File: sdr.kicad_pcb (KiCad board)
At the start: 4 copper layers, 65 x 30 mm, 136 parts, among them U1 FT601, U10 MIC94310, U11 PAM2305, U2 ESD7016, U3 LMS6002DR2, U4 ECP5, U5 Si5351, U6 PAM2305, U7 NCP186, U8 MIC94310, U9 MIC94310, X1 GSB443133HR, X2 CONN_01X08, X3 RaspberryPiConnector, Y1 FL3000027, Y2 ABM11-141-26.000MHZ

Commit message: All traced except Rpi and LMS
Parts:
- moved R6 6.61 mm to (124.7, 123.5)
- moved C77 2.49 mm to (153.6, 111.7)
- moved R7 1.64 mm to (125.1, 126.0)
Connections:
- net Net-(X3-Pad25) renamed /RPi/~RPI_WE
- net Net-(X3-Pad32) renamed /RPi/~RPI_OE
- U4 pad T17: /FT601/I2C_SCL -> Net-(U4-PadT17)
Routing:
- net ~CFG_HOLD: track 0.00 -> 74.0 mm, vias 0 -> 1
- net FT_GPIO1: track 19.5 -> 75.5 mm, vias 2 -> 3
- net LMS_D3V3: track 88.5 -> 125.4 mm, vias 17 -> 22
- net RPI_D13: track 0.00 -> 26.0 mm
- net CFG_MCLK: track 0.00 -> 25.1 mm, vias 0 -> 1
- net CFG_MISO: track 0.00 -> 23.5 mm, vias 0 -> 1
- net CFG_MOSI: track 0.00 -> 22.4 mm, vias 0 -> 1
- net RPI_D8: track 0.00 -> 21.8 mm
- net RPI_D12: track 0.00 -> 21.5 mm
- net RPI_D4: track 0.00 -> 19.2 mm
- net RPI_D11: track 0.00 -> 19.1 mm
- net RPI_D5: track 0.00 -> 18.6 mm
- net GNDD: track 235.4 -> 252.1 mm, vias 102 -> 104
- net /RPi/~RPI_OE: track 0.00 -> 15.6 mm
- net RPI_A4: track 0.00 -> 13.8 mm
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- added copper zone on F.Cu, net GNDD

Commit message: RPI is almost finished
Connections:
- U4 pad A10: Net-(U4-PadA10) -> RPI_D14
- U4 pad A11: Net-(U4-PadA11) -> RPI_D17
- U4 pad A12: Net-(U4-PadA12) -> RPI_A0
- U4 pad A13: Net-(U4-PadA13) -> /RPi/~RPI_OE
- U4 pad A14: Net-(U4-PadA14) -> RPI_D8
- U4 pad A16: Net-(U4-PadA16) -> RPI_D12
- U4 pad A7: Net-(U4-PadA7) -> RPI_A1
- U4 pad A8: Net-(U4-PadA8) -> RPI_D7
- U4 pad A9: Net-(U4-PadA9) -> RPI_D10
- U4 pad B11: Net-(U4-PadB11) -> RPI_D15
- U4 pad B12: Net-(U4-PadB12) -> RPI_A4
- U4 pad B13: Net-(U4-PadB13) -> RPI_D5
- U4 pad B16: Net-(U4-PadB16) -> RPI_D11
- U4 pad B8: Net-(U4-PadB8) -> RPI_D6
- U4 pad B9: Net-(U4-PadB9) -> RPI_D9
- U4 pad C10: Net-(U4-PadC10) -> RPI_GPIO1
- U4 pad C13: Net-(U4-PadC13) -> RPI_D4
- U4 pad E17: Net-(U4-PadE17) -> RPI_D13
- U4 pad F18: Net-(U4-PadF18) -> RPI_A5
- U4 pad G16: Net-(U4-PadG16) -> ~RPI_WE
- X3 pad 25: /RPi/~RPI_WE -> ~RPI_WE
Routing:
- net RPI_D6: track 0.00 -> 21.0 mm
- net RPI_D7: track 0.00 -> 18.0 mm
- net RPI_A1: track 0.00 -> 17.3 mm
- net RPI_D10: track 0.00 -> 16.5 mm
- net RPI_D9: track 0.00 -> 15.4 mm
- net RPI_A5: track 0.00 -> 14.5 mm, vias 0 -> 1
- net RPI_GPIO1: track 0.00 -> 14.2 mm
- net RPI_D15: track 0.00 -> 13.7 mm
- net ~RPI_WE: track 0.00 -> 13.4 mm, vias 0 -> 1
- net Net-(U4-PadF17): track 11.2 -> 0.02 mm, vias 1 -> 0
- net RPI_D14: track 0.00 -> 10.4 mm
- net Net-(U4-PadG18): track 9.79 -> 0.02 mm, vias 1 -> 0
- net RPI_D17: track 0.00 -> 8.65 mm
- net FT_GPIO1: track 75.5 -> 79.2 mm
- net RPI_CNTD: track 64.4 -> 66.5 mm
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
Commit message: Everything is done except LMS and RF
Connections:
- U4 pad A10: RPI_D14 -> RPI_GPIO1
- U4 pad A11: RPI_D17 -> RPI_D15
- U4 pad A12: RPI_A0 -> RPI_D17
- U4 pad A13: /RPi/~RPI_OE -> RPI_D4
- U4 pad A2: Net-(U4-PadA2) -> (no net)
- U4 pad A3: Net-(U4-PadA3) -> (no net)
- U4 pad A4: Net-(U4-PadA4) -> (no net)
- U4 pad A5: Net-(U4-PadA5) -> (no net)
- U4 pad A7: RPI_A1 -> RPI_A2
- U4 pad A8: RPI_D7 -> RPI_D6
- U4 pad A9: RPI_D10 -> RPI_D9
- U4 pad B1: Net-(U4-PadB1) -> (no net)
- U4 pad B10: Net-(U4-PadB10) -> RPI_D10
- U4 pad B11: RPI_D15 -> RPI_D14
- U4 pad B12: RPI_A4 -> RPI_D16
- U4 pad B15: Net-(U4-PadB15) -> RPI_A4
- U4 pad B2: Net-(U4-PadB2) -> (no net)
- U4 pad B3: Net-(U4-PadB3) -> (no net)
- U4 pad B4: Net-(U4-PadB4) -> (no net)
- U4 pad B5: Net-(U4-PadB5) -> (no net)
- U4 pad B8: RPI_D6 -> RPI_A1
- U4 pad B9: RPI_D9 -> RPI_D7
- U4 pad C1: Net-(U4-PadC1) -> (no net)
- U4 pad C10: RPI_GPIO1 -> Net-(U4-PadC10)
- U4 pad C13: RPI_D4 -> RPI_A0
- U4 pad C2: Net-(U4-PadC2) -> (no net)
- U4 pad C3: Net-(U4-PadC3) -> (no net)
- U4 pad C4: Net-(U4-PadC4) -> (no net)
- U4 pad C5: Net-(U4-PadC5) -> (no net)
- U4 pad C6: Net-(U4-PadC6) -> RPI_A3
- U4 pad D1: Net-(U4-PadD1) -> (no net)
- U4 pad D11: Net-(U4-PadD11) -> /RPi/~RPI_WE
- U4 pad D2: Net-(U4-PadD2) -> (no net)
- U4 pad D3: Net-(U4-PadD3) -> (no net)
- U4 pad D5: Net-(U4-PadD5) -> (no net)
- U4 pad E1: Net-(U4-PadE1) -> (no net)
- U4 pad E2: Net-(U4-PadE2) -> (no net)
- U4 pad E3: Net-(U4-PadE3) -> (no net)
- U4 pad E4: Net-(U4-PadE4) -> (no net)
- U4 pad E5: Net-(U4-PadE5) -> (no net)
- U4 pad F1: Net-(U4-PadF1) -> (no net)
- U4 pad F18: RPI_A5 -> ~RPI_OE
- U4 pad F2: Net-(U4-PadF2) -> (no net)
- U4 pad F3: Net-(U4-PadF3) -> (no net)
- U4 pad F4: Net-(U4-PadF4) -> (no net)
- U4 pad F5: Net-(U4-PadF5) -> (no net)
- U4 pad G1: Net-(U4-PadG1) -> (no net)
- U4 pad G16: ~RPI_WE -> RPI_A5
- U4 pad G2: Net-(U4-PadG2) -> (no net)
- U4 pad G3: Net-(U4-PadG3) -> (no net)
- U4 pad G5: Net-(U4-PadG5) -> (no net)
- U4 pad H1: Net-(U4-PadH1) -> (no net)
- U4 pad H2: Net-(U4-PadH2) -> (no net)
- U4 pad H3: Net-(U4-PadH3) -> (no net)
- U4 pad H4: Net-(U4-PadH4) -> (no net)
- U4 pad H5: Net-(U4-PadH5) -> (no net)
- U4 pad J1: Net-(U4-PadJ1) -> (no net)
- U4 pad J3: Net-(U4-PadJ3) -> (no net)
- U4 pad J4: Net-(U4-PadJ4) -> (no net)
- U4 pad J5: Net-(U4-PadJ5) -> (no net)
- U4 pad K1: Net-(U4-PadK1) -> (no net)
- U4 pad K2: Net-(U4-PadK2) -> (no net)
- U4 pad K3: Net-(U4-PadK3) -> (no net)
- U4 pad K4: Net-(U4-PadK4) -> (no net)
- U4 pad K5: Net-(U4-PadK5) -> (no net)
- U4 pad L1: Net-(U4-PadL1) -> (no net)
- U4 pad L2: Net-(U4-PadL2) -> (no net)
- U4 pad L3: Net-(U4-PadL3) -> (no net)
- U4 pad L4: Net-(U4-PadL4) -> (no net)
- U4 pad L5: Net-(U4-PadL5) -> (no net)
- U4 pad M1: Net-(U4-PadM1) -> (no net)
- U4 pad M3: Net-(U4-PadM3) -> (no net)
- U4 pad M4: Net-(U4-PadM4) -> (no net)
- U4 pad N1: Net-(U4-PadN1) -> (no net)
- U4 pad N2: Net-(U4-PadN2) -> (no net)
- U4 pad N3: Net-(U4-PadN3) -> (no net)
- U4 pad N4: Net-(U4-PadN4) -> (no net)
- U4 pad N5: Net-(U4-PadN5) -> (no net)
- U4 pad P1: Net-(U4-PadP1) -> (no net)
- U4 pad P2: Net-(U4-PadP2) -> (no net)
- U4 pad P3: Net-(U4-PadP3) -> (no net)
- U4 pad P4: Net-(U4-PadP4) -> (no net)
- U4 pad P5: Net-(U4-PadP5) -> (no net)
- U4 pad R1: (no net) -> Net-(U4-PadR1)
- U4 pad R3: (no net) -> Net-(U4-PadR3)
- U4 pad T1: (no net) -> Net-(U4-PadT1)
- U4 pad T3: (no net) -> Net-(U4-PadT3)
- U4 pad U1: (no net) -> Net-(U4-PadU1)
- U4 pad U2: (no net) -> Net-(U4-PadU2)
- U4 pad V1: (no net) -> Net-(U4-PadV1)
- U4 pad W1: (no net) -> Net-(U4-PadW1)
- U4 pad Y2: (no net) -> /FT601/I2C_SCL
- X3 pad 25: ~RPI_WE -> /RPi/~RPI_WE
- X3 pad 32: /RPi/~RPI_OE -> ~RPI_OE
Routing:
- net RPI_A3: track 0.00 -> 22.4 mm
- net RPI_A2: track 0.00 -> 19.6 mm
- net /RPi/~RPI_OE: track 16.0 -> 0.00 mm
- net ~RPI_WE: track 13.4 -> 0.00 mm, vias 1 -> 0
- net ~RPI_OE: track 0.00 -> 13.4 mm, vias 0 -> 1
- net /RPi/~RPI_WE: track 0.00 -> 12.8 mm, vias 0 -> 1
- net RPI_D16: track 0.00 -> 11.6 mm
- net RPI_A5: track 14.5 -> 11.9 mm
- net Net-(U4-PadD14): track 2.49 -> 0.02 mm, vias 1 -> 0
- net RPI_A4: track 14.3 -> 11.8 mm, vias 0 -> 1
- net RPI_D4: track 19.5 -> 17.6 mm
- net RPI_GPIO1: track 14.2 -> 12.4 mm
- net RPI_A1: track 17.3 -> 18.9 mm
- net RPI_D7: track 18.0 -> 19.6 mm
- net RPI_A0: track 13.4 -> 14.8 mm
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
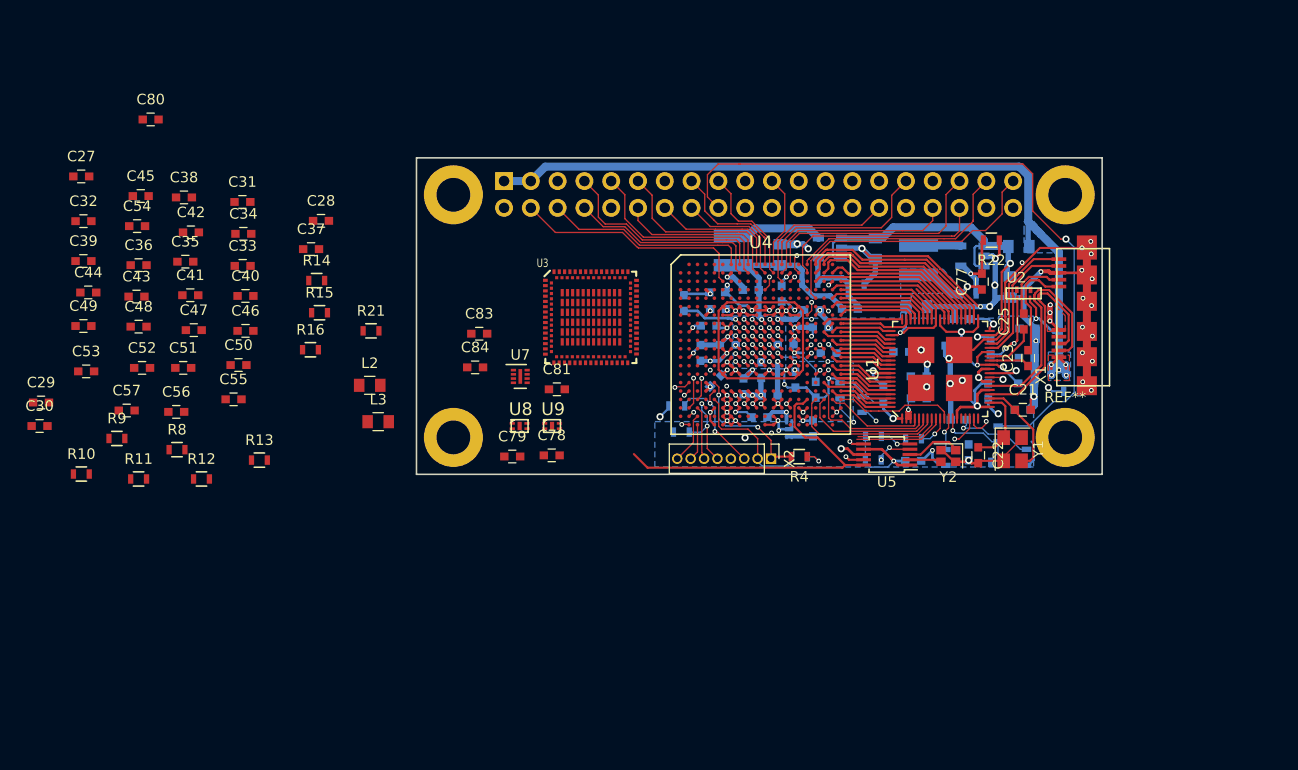
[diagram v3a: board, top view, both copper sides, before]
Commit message: Start placing RF. Shield is ready. Fixed some net bugs.
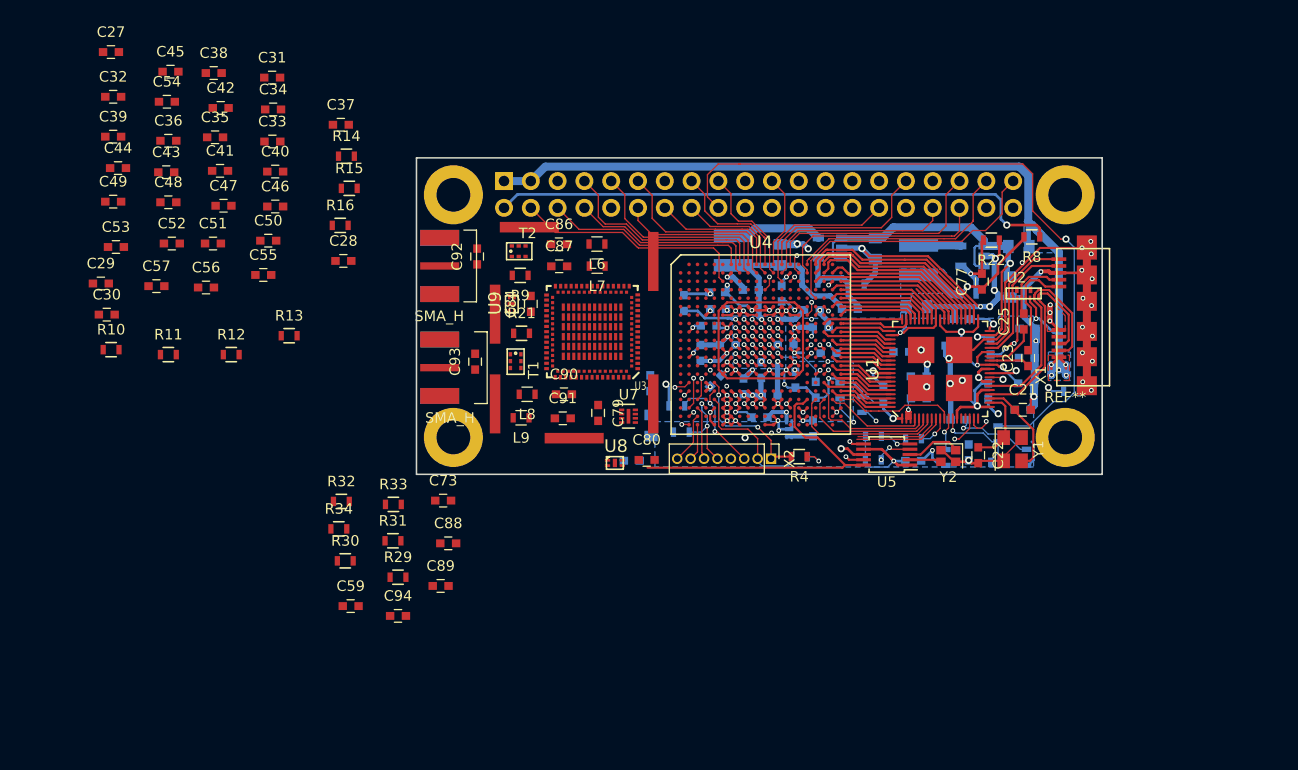
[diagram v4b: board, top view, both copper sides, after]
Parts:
- removed L2: BLM18KG601SN1D, Capacitors_SMD:C_0805
- added C59: 100n, Capacitors_SMD:C_0603, F.Cu at (93.8, 142.5)
- added C73: 100n, Capacitors_SMD:C_0603, F.Cu at (102.5, 132.5)
- added C86: 20p, Capacitors_SMD:C_0603, F.Cu at (113.5, 108.2)
- added C87: 20p, Capacitors_SMD:C_0603, F.Cu at (113.5, 110.3)
- added C88: 100p, Capacitors_SMD:C_0603, F.Cu at (103.0, 136.5)
- added C89: 100p, Capacitors_SMD:C_0603, F.Cu at (102.3, 140.6)
- added C90: 20p, Capacitors_SMD:C_0603, F.Cu at (114.0, 122.4)
- added C91: 20p, Capacitors_SMD:C_0603, F.Cu at (113.9, 124.7)
- added C92: 20p, Capacitors_SMD:C_0603, F.Cu at (105.8, 109.3)
- added C93: 20p, Capacitors_SMD:C_0603, F.Cu at (105.6, 119.3)
- added C94: 100p, Capacitors_SMD:C_0603, F.Cu at (98.2, 143.4)
- added J1: SMA_H, sdr-foots:SMA_H, F.Cu at (102.7, 119.9)
- added J2: SMA_H, sdr-foots:SMA_H, F.Cu at (101.7, 110.2)
- added L6: 36n, Inductors_SMD:L_0603, F.Cu at (117.1, 108.2)
- added L7: 36n, Inductors_SMD:L_0603, F.Cu at (117.1, 110.3)
- added L8: 2.7n, Inductors_SMD:L_0603, F.Cu at (110.5, 122.4)
- added L9: 2.7n, Inductors_SMD:L_0603, F.Cu at (109.9, 124.6)
- added R29: 22, Resistors_SMD:R_0603, F.Cu at (98.2, 139.8)
- added R30: 22, Resistors_SMD:R_0603, F.Cu at (93.2, 138.2)
- added R31: 22, Resistors_SMD:R_0603, F.Cu at (97.8, 136.3)
- added R32: 22, Resistors_SMD:R_0603, F.Cu at (92.9, 132.6)
- added R33: 22, Resistors_SMD:R_0603, F.Cu at (97.8, 132.8)
- added R34: 22, Resistors_SMD:R_0603, F.Cu at (92.6, 135.2)
- added REF**: shield, sdr-foots:shield, F.Cu at (107.5, 126.6)
- added T1: B0322J5050, sdr-foots:B0322J5050, F.Cu at (108.9, 119.9)
- added T2: B0322J5050, sdr-foots:B0322J5050, F.Cu at (110.3, 109.3)
- C10: value 100n -> 470n
- C11, C12, C13, C19, C2, C4, C64, C65, C66, C67: value 0.47u -> 470n
- C78, C81, C83, L3: moved to B.Cu
- moved R8 83.5 mm to (158.3, 107.5), turned to 180 degrees
- moved C80 57.0 mm to (121.8, 128.6)
- moved R9 41.2 mm to (109.8, 111.1), turned to 180 degrees
- moved L3 25.9 mm to (122.2, 125.4), turned to 90 degrees
- moved C83 18.8 mm to (120.4, 128.7)
- moved R21 14.3 mm to (110.0, 116.6)
- moved U3 13.3 mm to (121.0, 120.8), turned to 180 degrees
- moved C29 12.6 mm to (70.1, 111.9)
- moved C30 12.3 mm to (70.6, 114.9)
- moved U9 12.2 mm to (109.0, 113.9), turned to 90 degrees
- moved C27 12.1 mm to (71.0, 90.0)
- moved C36 12.1 mm to (76.5, 98.4)
- moved C38 12.1 mm to (80.8, 92.0)
- moved C43 12.1 mm to (76.3, 101.4)
- moved C45 12.1 mm to (76.7, 91.8)
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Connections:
- C27 pad 2: LMS_D1V8 -> LMS_D3V3
- C29 pad 1: Net-(C29-Pad1) -> GNDD
- C29 pad 2: LMS_D1V8 -> LMS_D3V3
- C3 pad 1: LMS_D1V8 -> LMS_D3V3
- C32 pad 2: LMS_D1V8 -> LMS_D3V3
- C35 pad 1: Net-(C35-Pad1) -> LMS_D1V8
- C38 pad 1: Net-(C35-Pad1) -> LMS_D1V8
- C44 pad 1: Net-(C44-Pad1) -> LMS_A3V3
- C46 pad 1: Net-(C44-Pad1) -> LMS_A3V3
- C47 pad 1: Net-(C44-Pad1) -> LMS_A3V3
- C48 pad 2: Net-(C44-Pad1) -> LMS_A3V3
- C50 pad 1: Net-(C44-Pad1) -> LMS_A3V3
- C51 pad 1: Net-(C44-Pad1) -> LMS_A3V3
- C52 pad 1: Net-(C44-Pad1) -> LMS_A3V3
- C53 pad 2: Net-(C44-Pad1) -> LMS_A3V3
- C54 pad 1: Net-(C44-Pad1) -> LMS_A3V3
- C55 pad 1: Net-(C44-Pad1) -> LMS_A3V3
- C78 pad 1: LMS_D3V3 -> Net-(C78-Pad1)
- C78 pad 2: Net-(C78-Pad2) -> GNDD
- C79 pad 1: LMS_A3V3 -> Net-(C79-Pad1)
- C79 pad 2: Net-(C78-Pad2) -> GNDD
- C81 pad 1: LMS_D3V3 -> LMS_A3V3
- L3 pad 1: LMS_A3V3 -> LMS_D3V3
- L3 pad 2: Net-(C44-Pad1) -> Net-(C78-Pad1)
- R21 pad 1: Net-(L2-Pad2) -> LMS_A1V8
- R9 pad 2: Net-(L2-Pad2) -> LMS_A1V8
- U3 pad 1: LMS_D1V8 -> LMS_D3V3
- U3 pad 101: Net-(C44-Pad1) -> LMS_A3V3
- U3 pad 107: Net-(C44-Pad1) -> LMS_A3V3
- U3 pad 109: Net-(C44-Pad1) -> LMS_A3V3
- U3 pad 111: Net-(C44-Pad1) -> LMS_A3V3
- U3 pad 112: Net-(C44-Pad1) -> LMS_A3V3
- U3 pad 12: LMS_D1V8 -> LMS_D3V3
- U3 pad 18: LMS_D1V8 -> LMS_D3V3
- U3 pad 34: LMS_D1V8 -> LMS_D3V3
- U3 pad 37: Net-(C44-Pad1) -> LMS_A3V3
- U3 pad 43: Net-(C44-Pad1) -> LMS_A3V3
- U3 pad 45: Net-(C44-Pad1) -> LMS_A3V3
- U3 pad 47: Net-(C44-Pad1) -> LMS_A3V3
- U3 pad 49: Net-(C44-Pad1) -> LMS_A3V3
- U3 pad 58: Net-(C44-Pad1) -> LMS_A3V3
- U3 pad 59: Net-(C44-Pad1) -> LMS_A3V3
- U3 pad 61: Net-(C35-Pad1) -> LMS_D1V8
- U3 pad 62: Net-(C44-Pad1) -> LMS_A3V3
- U3 pad 63: Net-(C44-Pad1) -> LMS_A3V3
- U3 pad 74: LMS_D1V8 -> LMS_D3V3
- U3 pad 78: Net-(C44-Pad1) -> LMS_A3V3
- U3 pad 79: Net-(C44-Pad1) -> LMS_A3V3
- U3 pad 81: Net-(C44-Pad1) -> LMS_A3V3
- U3 pad 82: Net-(C44-Pad1) -> LMS_A3V3
- U3 pad 85: Net-(C44-Pad1) -> LMS_A3V3
- U3 pad 86: Net-(C44-Pad1) -> LMS_A3V3
- U3 pad 90: Net-(C44-Pad1) -> LMS_A3V3
- U3 pad 97: Net-(U3-Pad97) -> GNDD
- U3 pad 99: Net-(U3-Pad99) -> GNDD
- U4 pad H6: LMS_D1V8 -> LMS_D3V3
- U4 pad H7: LMS_D1V8 -> LMS_D3V3
- U4 pad J6: LMS_D1V8 -> LMS_D3V3
- U7 pad 1: LMS_A3V3 -> Net-(U7-Pad1)
- U7 pad 2: LMS_A3V3 -> Net-(U7-Pad1)
- U7 pad 3: Net-(C78-Pad2) -> GNDD
- U7 pad 4: LMS_A3V3 -> Net-(U7-Pad1)
- U7 pad 5: Net-(C78-Pad2) -> GNDD
- U7 pad 6: LMS_D3V3 -> Net-(C78-Pad1)
- U7 pad 7: LMS_D3V3 -> Net-(C78-Pad1)
- U7 pad 8: LMS_D3V3 -> Net-(C78-Pad1)
- U7 pad 9: Net-(C78-Pad2) -> GNDD
- U9 pad 3: LMS_D3V3 -> LMS_A3V3
- U9 pad 4: LMS_D3V3 -> LMS_A3V3
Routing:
- net Net-(R8-Pad1): track 0.00 -> 54.5 mm, vias 0 -> 1
- net LMS_D3V3: track 125.4 -> 134.9 mm, vias 22 -> 23
- net LMS_D1V8: track 2.81 -> 0.00 mm, vias 1 -> 0
- net CLK0: track 33.0 -> 31.2 mm
- net ~CFG_HOLD: track 74.0 -> 75.5 mm
- net GNDD: track 252.8 -> 254.1 mm
